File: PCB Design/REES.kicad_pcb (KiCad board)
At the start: 2 copper layers, 141 x 80 mm, 37 parts, among them J1 Screw_Terminal_01x02, Q1 BC547, SW1 ENCODER_SW1-PEC12

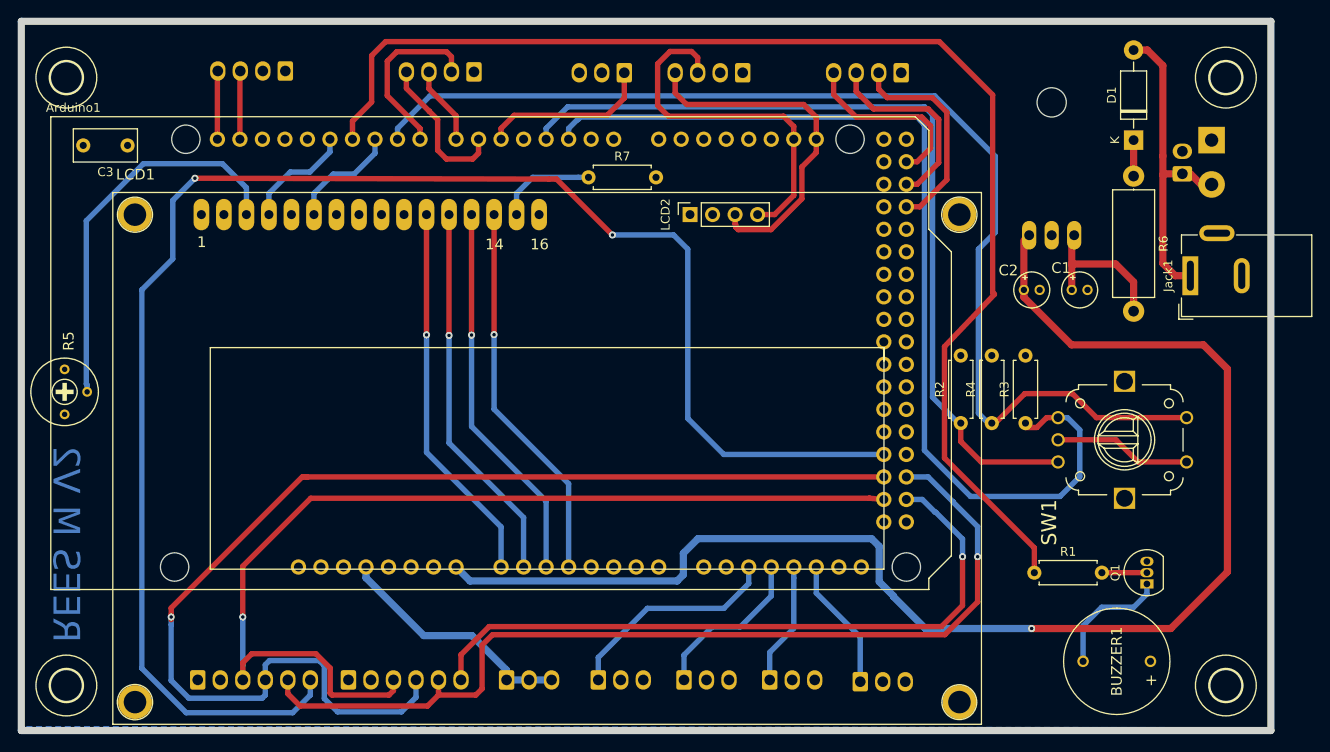
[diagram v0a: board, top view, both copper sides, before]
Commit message: PCB Silkscreen modified
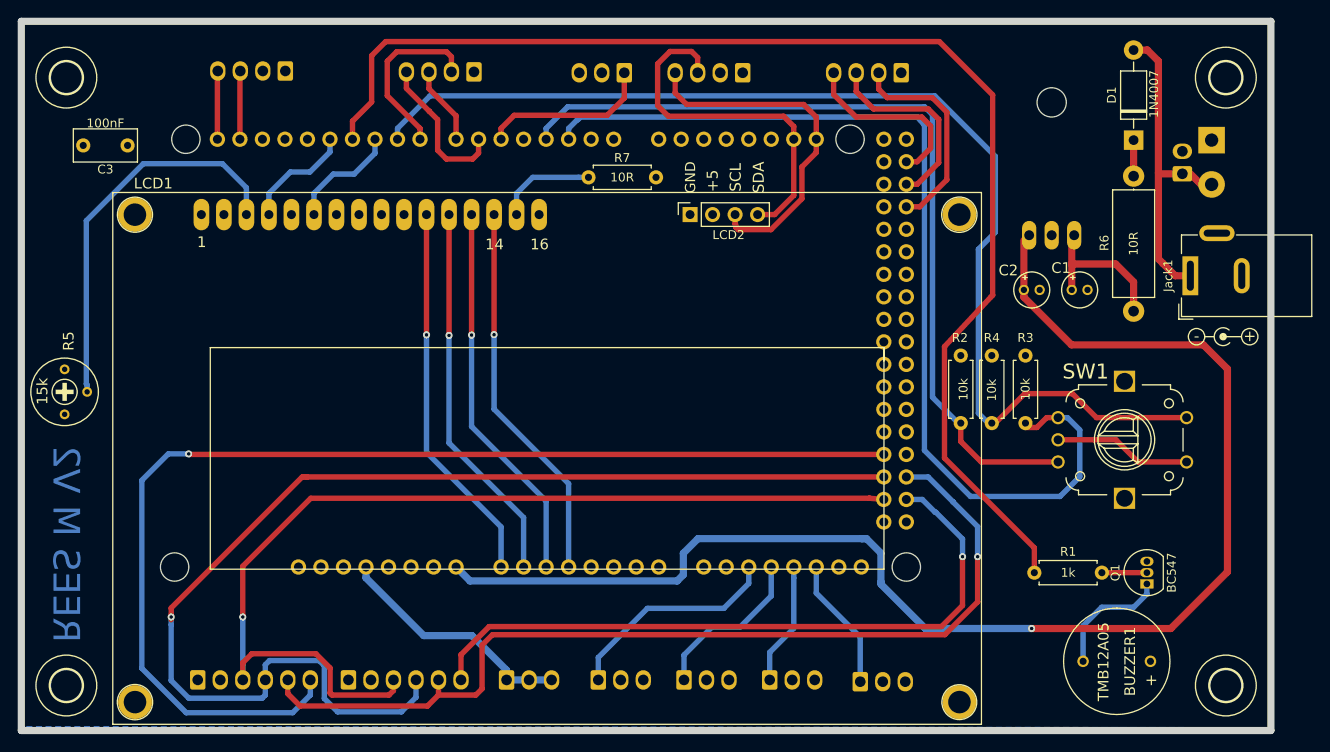
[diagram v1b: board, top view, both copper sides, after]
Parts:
- added REF**: Symbol_Barrel_Polarity, Symbol:Symbol_Barrel_Polarity, F.Cu at (213.6, 100.5)
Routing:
- net /SS1: track 183.3 -> 129.8 mm, vias 2 -> 1
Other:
- board text added: "+3.3V"
- board text added: "+5"
- board text added: "-"
- board text added: "A10"
- board text added: "A11"
- board text added: "A12"
- board text added: "A13"
- board text added: "DIR"
- board text added: "EN"
- board text added: "GND"
- board text added: "HALL"
- board text added: "MISO"
- board text added: "MOSI"
- board text added: "PUL"
- board text added: "SCK"
- board text added: "SCL"
- board text added: "SDA"
- board text added: "SS0"
- board text added: "SS1"
- board text added: "VCC"
